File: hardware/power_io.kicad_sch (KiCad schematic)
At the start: 6 parts, among them J4 Conn_T7_Analog, J6 Conn_Power

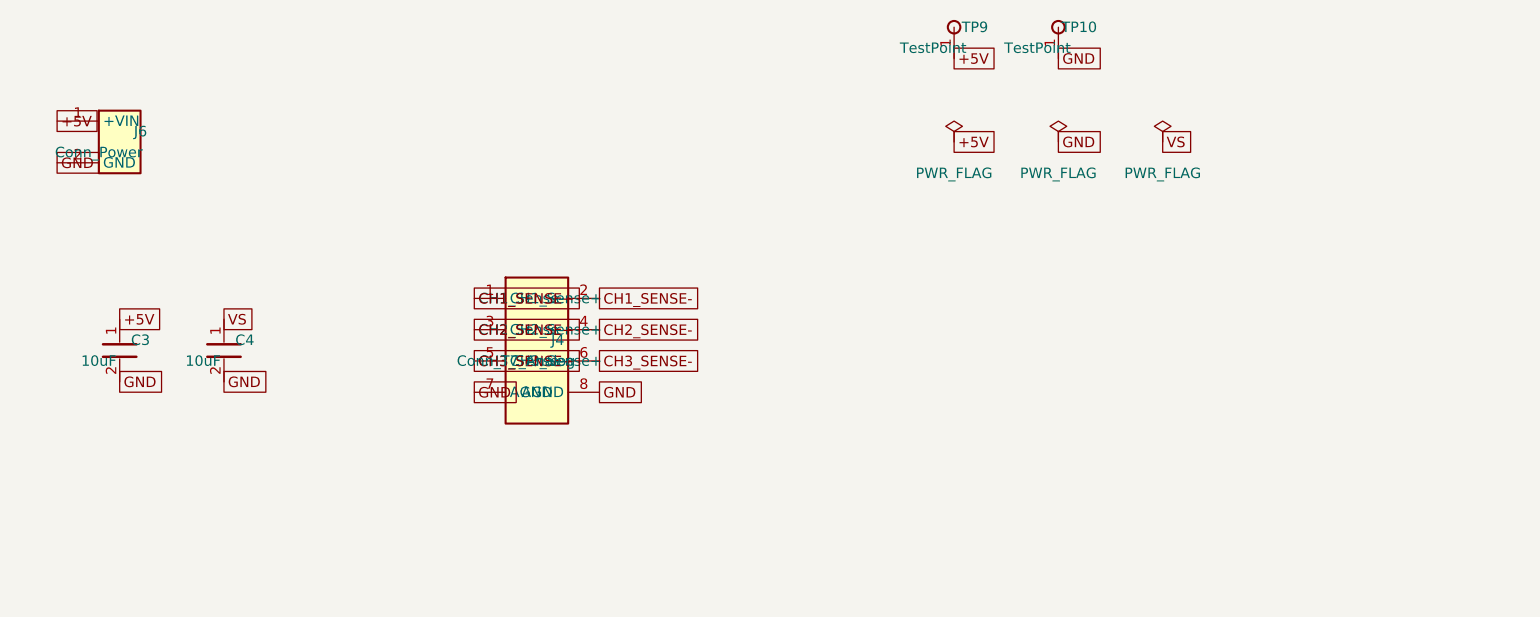
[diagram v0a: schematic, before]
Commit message: trackE: wire-up pass -- drawn wires + power symbols (netlist unchanged)
Convert the label-based capture to a conventionally drawn schematic: unit cells
as a drawn series current-loop (+5V/GND power symbols, CRD->R_ref->RTD, tapped
TOP/MID to TPs+labels); acquisition/power_io pins stub to power symbols/labels;
cross-sheet signals stay labelled. Fixed a y-down rotation bug (CRD anode/cathode
swap) by rotating the CRD 90 not 270.

ERC 0 errors / 0 warnings. Netlist node-for-node IDENTICAL to the pre-wiring
verified netlist (21 nets, diff empty); sim/netlists refreshed.

Co-Authored-By: Claude Opus 4.8 <noreply@anthropic.com>
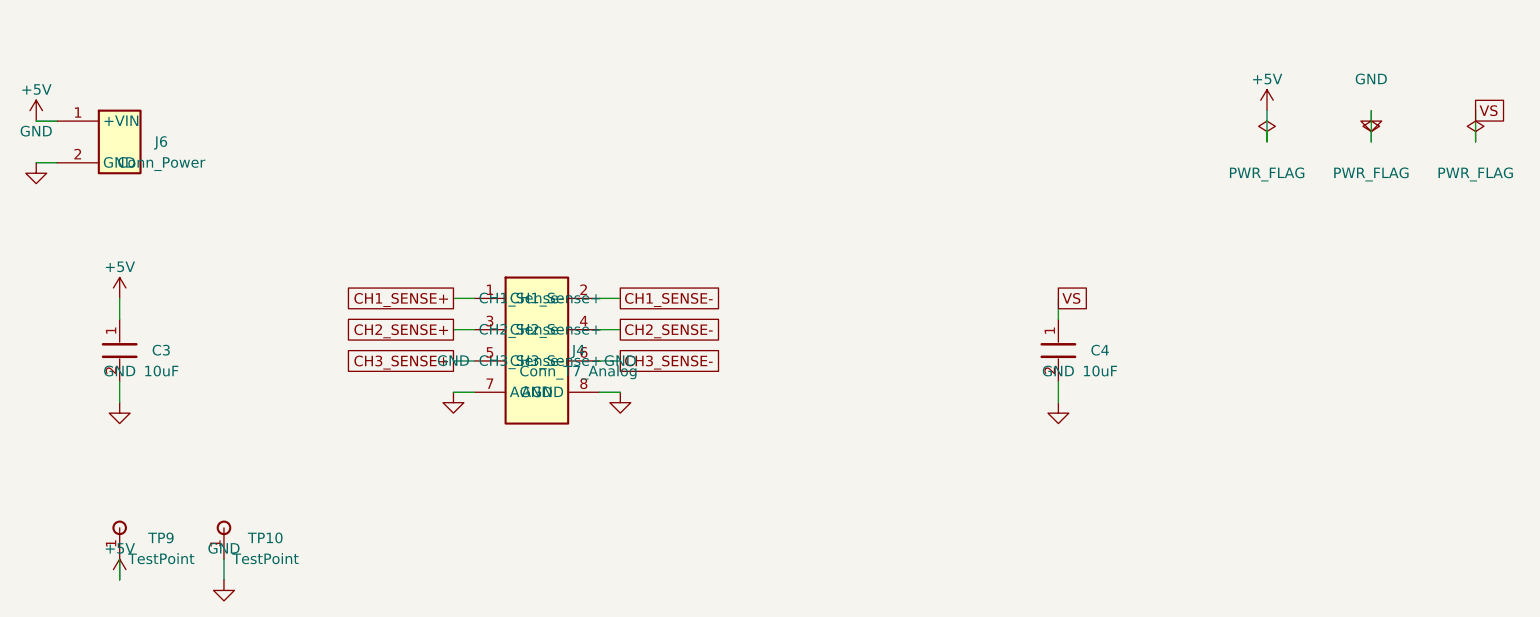
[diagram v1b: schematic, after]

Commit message: rev-B: real Digi-Key parts + layout review (copper unchanged)
Independent layout review + adversarial verify: 4-layer split planes, single-
point analog/digital GND tie, Kelvin intact -> fabricable (yes-with-fixes).
Real Digi-Key MPNs on the whole BOM; fixed RTD conn P/N (1729160 6-pos ->
1729144 4-pos) and R_ref tempco (25ppm -> Vishay TNPU1206 <=10ppm per spec).
ERC 0/0, DRC 0/0. Open decision: sense-line RC filter (see USER_MANUAL 8.5).

Co-Authored-By: Claude Opus 4.8 <noreply@anthropic.com>
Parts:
- C3, C4: MPN (set per value at BOM time) -> GRM188R61E106KA73D; Manufacturer (generic) -> Murata
- J4: MPN (2x4 2.54 mm header) -> PREC004DAAN-RC (2x4; confirm); Manufacturer (generic) -> Sullins
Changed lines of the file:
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@@
 			)
 		)
-		(property "MPN" "(2x4 2.54 mm header)"
+		(property "MPN" "PREC004DAAN-RC (2x4; confirm)"
 			(at 101.6 76.2 0)
 			(show_name no)
@@
 			)
 		)
-		(property "Manufacturer" "(generic)"
+		(property "Manufacturer" "Sullins"
 			(at 101.6 76.2 0)
 			(show_name no)
@@
 			)
 		)
-		(property "MPN" "(set per value at BOM time)"
-			(at 50.8 76.2 0)
-			(show_name no)
-			(do_not_autoplace no)
-			(hide yes)
-			(effects
-				(font
-					(size 1.27 1.27)
-				)
-			)
-		)
-		(property "Manufacturer" "(generic)"
+		(property "MPN" "GRM188R61E106KA73D"
+			(at 50.8 76.2 0)
+			(show_name no)
+			(do_not_autoplace no)
+			(hide yes)
+			(effects
+				(font
+					(size 1.27 1.27)
+				)
+			)
+		)
+		(property "Manufacturer" "Murata"
 			(at 50.8 76.2 0)
 			(show_name no)
@@
 			)
 		)
-		(property "MPN" "(set per value at BOM time)"
-			(at 165.1 76.2 0)
-			(show_name no)
-			(do_not_autoplace no)
-			(hide yes)
-			(effects
-				(font
-					(size 1.27 1.27)
-				)
-			)
-		)
-		(property "Manufacturer" "(generic)"
-			(at 165.1 76.2 0)
-			(show_name no)
+		(property "MPN" "GRM188R61E106KA73D"
+			(at 165.1 76.2 0)
+			(show_name no)
+			(do_not_autoplace no)
+			(hide yes)
+			(effects
+				(font
+					(size 1.27 1.27)
+				)
+			)
+		)
+		(property "Manufacturer" "Murata"
+			(at 165.1 76.2 0)
+			(show_name no)
